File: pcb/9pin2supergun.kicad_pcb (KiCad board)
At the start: 4 copper layers, 49.5 x 50.5 mm, 47 parts, among them J1 DA15_Receptacle, J2 Controller Input, J3 Debug (JST SH), J4 Debug (2.54mm holes), J5 UJ20-C-H-C-4-SMT-TR, SW1 09.10201.02, U1 NCP1117-3.3_SOT223, U2 W25Q128JVS, U3 RP2040, U4 R-667995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

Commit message: Update the schematic to properly use hierarchical sheets, update the PCB to match, tidy up some weirdnesses (button with a "U" refdes, both S and SW refdes, etc)
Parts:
- C50: value 0.1uF -> 100n
- renumbered SW1 to S2, U4 to S3
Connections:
- net /3.3v Down/Y renamed /Project components/3.3v Down/Y
- net /3.3v Fire 1/Clock/B/A renamed /Project components/3.3v Fire 1/Clock/B/A
- net /3.3v Fire 2/Data/C/Start renamed /Project components/3.3v Fire 2/Data/C/Start
- net /3.3v Latch/Power renamed /Project components/3.3v Latch/Power
- net /3.3v Left/X/GND renamed /Project components/3.3v Left/X/GND
- net /3.3v Power/Select renamed /Project components/3.3v Power/Select
- net /3.3v Right/Mode/GND renamed /Project components/3.3v Right/Mode/GND
- net /3.3v Up/Z renamed /Project components/3.3v Up/Z
- net /5v Down/Y renamed /Project components/5v Down/Y
- net /5v Fire 1/Clock/B/A renamed /Project components/5v Fire 1/Clock/B/A
- net /5v Fire 2/Data/C/Start renamed /Project components/5v Fire 2/Data/C/Start
- net /5v Latch/Power renamed /Project components/5v Latch/Power
- net /5v Left/X/GND renamed /Project components/5v Left/X/GND
- net /5v Power/Select renamed /Project components/5v Power/Select
- net /5v Right/Mode/GND renamed /Project components/5v Right/Mode/GND
- net /5v Up/Z renamed /Project components/5v Up/Z
- net /Button renamed /Project components/Button
- net /Button 1 renamed /Project components/Button 1
- net /Button 2 renamed /Project components/Button 2
- net /Button 3 renamed /Project components/Button 3
- net /Button 4 renamed /Project components/Button 4
- net /Button 5 renamed /Project components/Button 5
- net /Button 6 renamed /Project components/Button 6
- net /Coin renamed /Project components/Coin
- net /Down renamed /Project components/Down
- net /Left renamed /Project components/Left
- net /Mode switch renamed /Project components/Mode switch
- net /Pin 6 Dir renamed /Project components/Pin 6 direction
- net /QSPI_SCLK renamed /RP2040 Support/QSPI_SCLK
- net /QSPI_SD0 renamed /RP2040 Support/QSPI_SD0
- net /QSPI_SD1 renamed /RP2040 Support/QSPI_SD1
- net /QSPI_SD2 renamed /RP2040 Support/QSPI_SD2
- net /QSPI_SD3 renamed /RP2040 Support/QSPI_SD3
- net /QSPI_SS renamed /RP2040 Support/QSPI_SS
- net /Right renamed /Project components/Right
- net /SWCLK renamed /RP2040 Support/SWCLK
- net /SWD renamed /RP2040 Support/SWD
- net /Start renamed /Project components/Start
- net /Up renamed /Project components/Up
- net /XIN renamed /RP2040 Support/XIN
- net /XOUT renamed /RP2040 Support/XOUT
- net /~{OE} renamed /Project components/~{OE}
- net /~{USB_BOOT} renamed /RP2040 Support/~{USB_BOOT}
- D1 pad 1: /LED control -> /Project components/LED Control
- U3 pad 27: /LED control -> /Project components/LED Control

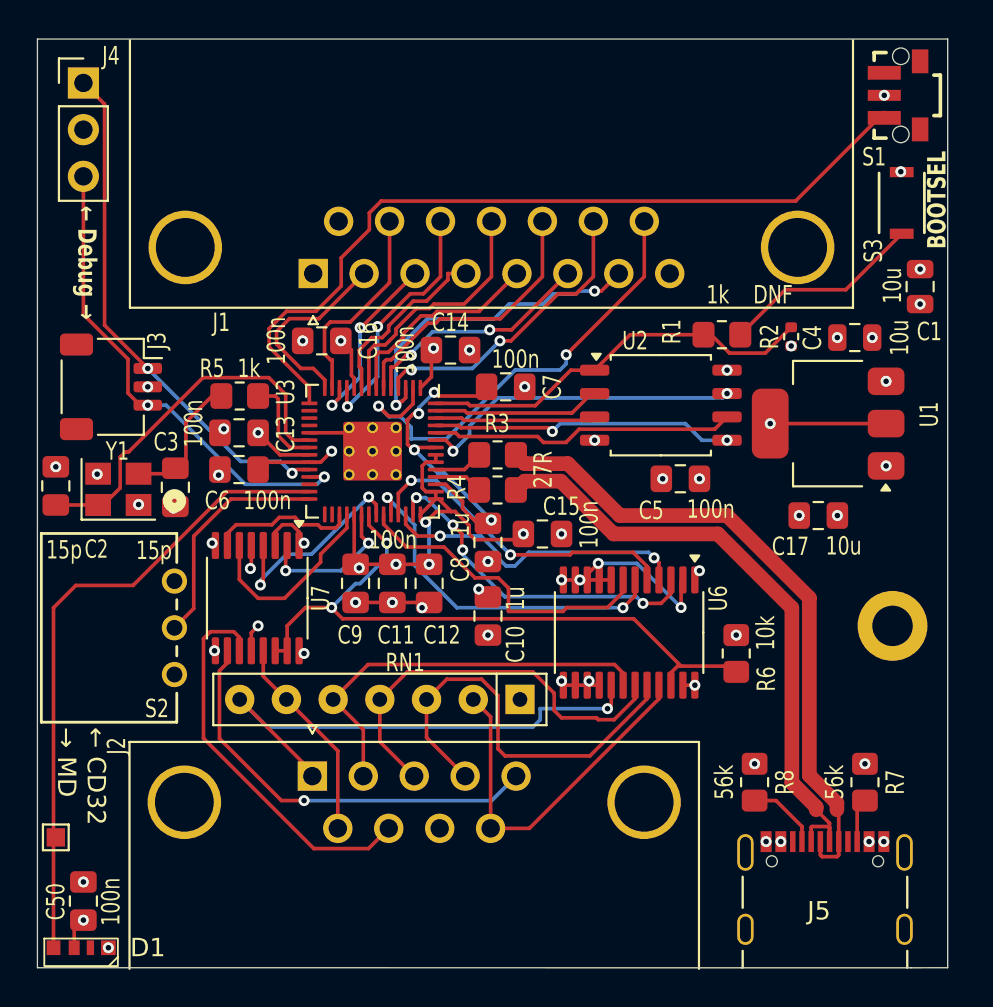
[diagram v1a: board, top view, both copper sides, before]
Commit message: Update PCB to v1.1:  * Update level shifting to a component that actually supports 5V  * Make both D-Sub connectors the same size in terms of pin offset (added bonus of making the board smaller)  * Update a couple of footprints that have changed name  * Add a switch for USB host/device,
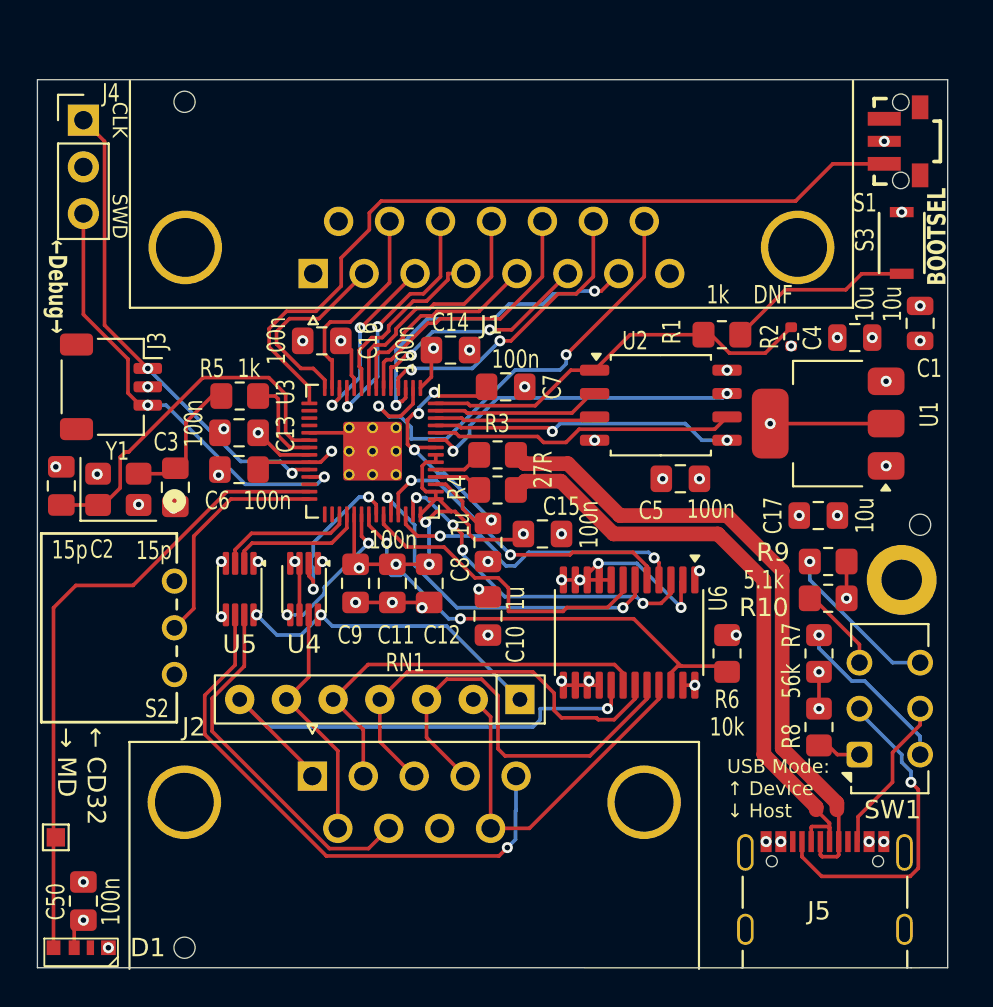
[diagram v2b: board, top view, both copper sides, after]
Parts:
- removed U7: SN74AVC4T245PW, Package_SO:TSSOP-16_4.4x5mm_P0.65mm
- added R10: 5.1k, Resistor_SMD:R_0805_2012Metric_Pad1.20x1.40mm_HandSolder, F.Cu at (181.5, 104.5)
- added R9: 5.1k, Resistor_SMD:R_0805_2012Metric_Pad1.20x1.40mm_HandSolder, F.Cu at (181.5, 102.5)
- added REF**: ToolingHole_1.152mm, MountingHole:ToolingHole_1.152mm, F.Cu at (146.5, 123.5)
- added REF**: ToolingHole_1.152mm, MountingHole:ToolingHole_1.152mm, F.Cu at (146.5, 77.5)
- added REF**: ToolingHole_1.152mm, MountingHole:ToolingHole_1.152mm, F.Cu at (186.5, 100.5)
- added SW1: SW_DPDT_x2, Button_Switch_THT:SW_CK_JS202011CQN_DPDT_Straight, F.Cu at (183.2, 113.0)
- added U4: SN74LVC2T45DCUR, Package_SO:VSSOP-8_2.3x2mm_P0.5mm, F.Cu at (153.0, 104.0)
- added U5: SN74LVC2T45DCUR, Package_SO:VSSOP-8_2.3x2mm_P0.5mm, F.Cu at (149.5, 104.0)
- J1: value DA15_Receptacle -> Controller Output; footprint Connector_Dsub:DSUB-15_Female_Horizontal_P2.77x2.84mm_EdgePinOffset9.90mm_Housed_MountingHolesOffset11.32mm -> Connector_Dsub:DSUB-15_Socket_Horizontal_P2.77x2.84mm_EdgePinOffset7.70mm_Housed_MountingHolesOffset9.12mm
- J2: footprint Connector_Dsub:DSUB-9_Male_Horizontal_P2.77x2.84mm_EdgePinOffset7.70mm_Housed_MountingHolesOffset9.12mm -> Connector_Dsub:DSUB-9_Pins_Horizontal_P2.77x2.84mm_EdgePinOffset7.70mm_Housed_MountingHolesOffset9.12mm
- moved R7 7.43 mm to (181.0, 107.5), turned to 90 degrees
- moved R8 4.61 mm to (181.0, 111.5)
- moved REF** 2.55 mm to (185.5, 103.5)
- moved S1 2.50 mm to (185.4, 79.7)
- moved S3 2.18 mm to (185.5, 85.2)
- moved J4 2.03 mm to (141.0, 78.5)
- moved C1 2.00 mm to (186.5, 89.5)
- moved QR***** 1.80 mm to (178.0, 107.5)
- moved R6 0.50 mm to (176.0, 107.5)
- moved C2 0.30 mm to (139.8, 98.4)
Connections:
- R7 pad 2: Net-(J5-CC2) -> Net-(SW1B-C)
- R8 pad 2: Net-(J5-CC1) -> Net-(SW1A-A)
- REF** pad 1: /LED control -> /Project components/LED Control
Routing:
- net /Project components/LED Control: track 0.00 -> 35.0 mm
- net /LED control: track 35.0 -> 0.00 mm
- net VBUS: track 0.65 -> 19.8 mm, vias 8 -> 9
- net Net-(J5-CC1): track 3.98 -> 17.8 mm, vias 0 -> 1
- net /Project components/~{OE}: track 36.5 -> 26.3 mm
- net Net-(SW1B-C): track 0.00 -> 9.19 mm, vias 0 -> 1
- net Net-(SW1B-A): track 0.00 -> 8.86 mm, vias 0 -> 1
- net /Project components/5v Latch/Power: track 23.0 -> 30.6 mm
- net Net-(J5-CC2): track 2.41 -> 8.65 mm
- net Net-(SW1A-C): track 0.00 -> 4.73 mm
- net /Project components/3.3v Power/Select: track 10.7 -> 7.51 mm
- net +3.3V: track 41.9 -> 38.8 mm, vias 19 -> 21
- net Net-(SW1A-A): track 0.00 -> 2.41 mm
- net /Project components/3.3v Fire 1/Clock/B/A: track 11.3 -> 9.26 mm
- net /RP2040 Support/SWCLK: track 28.2 -> 26.2 mm
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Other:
- board size 49.5 x 50.5 mm -> 49.5 x 48.3 mm
- board text added: "5.1k"
- board text added: "CLK"
- board text added: "PCB v1.1"
- board text added: "SWD"
- board text added: "USB Mode: ↑ Device ↓ Host"
- board text added: "https://github.com/turmoni/9pin2supergun Code and board by Dave Wickham"
- board text added: "←Debug→"
- board text removed: "PCB v1.0"
- board text removed: "Will not work with a PC and a C-C cable! Use A-C"
- board text removed: "https://github.com/turmoni/9pin2supergun Code and board by Dave Wickham This probably won't blow anything up, but use at your own risk"
- board text removed: "← Debug →"
